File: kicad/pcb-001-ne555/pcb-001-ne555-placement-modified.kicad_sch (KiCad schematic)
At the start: 14 parts, among them J1 +5 V / GND power input, U1 NE555D

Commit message: Update project files 2026-08-16 01:39:38
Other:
- moved on the sheet: R3
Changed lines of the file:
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@@
+	)
+	(junction
+		(at 194.31 102.87)
+		(diameter 0)
+		(color 0 0 0 0)
 	)
 	(junction
@@
 	)
 	(junction
-		(at 194.31 102.87)
-		(diameter 0)
-		(color 0 0 0 0)
-	)
-	(junction
 		(at 129.54 99.06)
 		(diameter 0)
@@
 	(wire
 		(pts
+			(xy 194.31 102.87) (xy 198.12 102.87)
+		)
+		(stroke
+			(width 0)
+			(type default)
+		)
+	)
+	(wire
+		(pts
 			(xy 186.69 102.87) (xy 194.31 102.87)
 		)
@@
 	(wire
 		(pts
-			(xy 209.55 102.87) (xy 209.55 106.68)
-		)
-		(stroke
-			(width 0)
-			(type default)
-		)
-	)
-	(wire
-		(pts
-			(xy 194.31 102.87) (xy 200.66 102.87)
+			(xy 207.01 102.87) (xy 207.01 106.68)
 		)
 		(stroke
@@
 	(wire
 		(pts
-			(xy 208.28 102.87) (xy 209.55 102.87)
+			(xy 205.74 102.87) (xy 207.01 102.87)
 		)
 		(stroke
@@
 		)
 		(instances
-			(project "pcb-001-ne555"
+			(project "pcb-001-ne555-placement-modified"
 				(path "/b0c8241f-7280-4983-bb24-fcd4e712ed60"
 					(reference "#PWR04")
@@
 		)
 		(instances
-			(project "pcb-001-ne555"
+			(project "pcb-001-ne555-placement-modified"
 				(path "/b0c8241f-7280-4983-bb24-fcd4e712ed60"
 					(reference "U1")
@@
 		)
 		(property "Value" "PWR_FLAG"
-			(at 145.796 110.744 0)
+			(at 145.288 110.744 0)
 			(show_name no)
 			(do_not_autoplace no)
@@
 		)
 		(instances
-			(project "pcb-001-ne555"
+			(project "pcb-001-ne555-placement-modified"
 				(path "/b0c8241f-7280-4983-bb24-fcd4e712ed60"
 					(reference "#FLG01")
@@
 		)
 		(instances
-			(project "pcb-001-ne555"
+			(project "pcb-001-ne555-placement-modified"
 				(path "/b0c8241f-7280-4983-bb24-fcd4e712ed60"
 					(reference "TP1")
@@
 		)
 		(instances
-			(project "pcb-001-ne555"
+			(project "pcb-001-ne555-placement-modified"
 				(path "/b0c8241f-7280-4983-bb24-fcd4e712ed60"
 					(reference "C3")
@@
 	(symbol
 		(lib_id "power:GND")
-		(at 209.55 106.68 0)
+		(at 207.01 106.68 0)
 		(unit 1)
 		(body_style 1)
@@
 		(fields_autoplaced yes)
 		(property "Reference" "#PWR010"
-			(at 209.55 113.03 0)
+			(at 207.01 113.03 0)
 			(hide yes)
 			(show_name no)
@@
 		)
 		(property "Value" "GND"
-			(at 209.55 111.76 0)
+			(at 207.01 111.76 0)
 			(show_name no)
 			(do_not_autoplace no)
@@
 		)
 		(property "Footprint" ""
-			(at 209.55 106.68 0)
+			(at 207.01 106.68 0)
 			(hide yes)
 			(show_name no)
@@
 		)
 		(property "Datasheet" ""
-			(at 209.55 106.68 0)
+			(at 207.01 106.68 0)
 			(hide yes)
 			(show_name no)
@@
 		)
 		(property "Description" "Power symbol creates a global label with name \"GND\" , ground"
-			(at 209.55 106.68 0)
+			(at 207.01 106.68 0)
 			(hide yes)
 			(show_name no)
@@
 		)
 		(instances
-			(project "pcb-001-ne555"
+			(project "pcb-001-ne555-placement-modified"
 				(path "/b0c8241f-7280-4983-bb24-fcd4e712ed60"
 					(reference "#PWR010")
@@
 		)
 		(instances
-			(project "pcb-001-ne555"
+			(project "pcb-001-ne555-placement-modified"
 				(path "/b0c8241f-7280-4983-bb24-fcd4e712ed60"
 					(reference "C2")
@@
 		)
 		(instances
-			(project "pcb-001-ne555"
+			(project "pcb-001-ne555-placement-modified"
 				(path "/b0c8241f-7280-4983-bb24-fcd4e712ed60"
 					(reference "R2")
@@
 		)
 		(instances
-			(project "pcb-001-ne555"
+			(project "pcb-001-ne555-placement-modified"
 				(path "/b0c8241f-7280-4983-bb24-fcd4e712ed60"
 					(reference "R1")
@@
 		)
 		(instances
-			(project "pcb-001-ne555"
+			(project "pcb-001-ne555-placement-modified"
 				(path "/b0c8241f-7280-4983-bb24-fcd4e712ed60"
 					(reference "TP3")
@@
 	(symbol
 		(lib_id "Device:R")
-		(at 204.47 102.87 90)
+		(at 201.93 102.87 90)
 		(unit 1)
 		(body_style 1)
@@
 		(fields_autoplaced yes)
 		(property "Reference" "R3"
-			(at 204.47 96.52 90)
+			(at 201.93 96.52 90)
 			(show_name no)
 			(do_not_autoplace no)
@@
 		)
 		(property "Value" "330 Ohm"
-			(at 204.47 99.06 90)
+			(at 201.93 99.06 90)
 			(show_name no)
 			(do_not_autoplace no)
@@
 		)
 		(property "Footprint" "Resistor_THT:R_Axial_DIN0207_L6.3mm_D2.5mm_P10.16mm_Horizontal"
-			(at 204.47 104.648 90)
+			(at 201.93 104.648 90)
 			(hide yes)
 			(show_name no)
@@
 		)
 		(property "Datasheet" ""
-			(at 204.47 102.87 0)
+			(at 201.93 102.87 0)
 			(hide yes)
 			(show_name no)
@@
 		)
 		(property "Description" "Resistor"
-			(at 204.47 102.87 0)
+			(at 201.93 102.87 0)
 			(hide yes)
 			(show_name no)
@@
 		)
 		(instances
-			(project "pcb-001-ne555"
+			(project "pcb-001-ne555-placement-modified"
 				(path "/b0c8241f-7280-4983-bb24-fcd4e712ed60"
 					(reference "R3")
@@
 		)
 		(instances
-			(project "pcb-001-ne555"
+			(project "pcb-001-ne555-placement-modified"
 				(path "/b0c8241f-7280-4983-bb24-fcd4e712ed60"
 					(reference "TP2")
@@
 		)
 		(property "Value" "PWR_FLAG"
-			(at 136.906 118.618 0)
+			(at 140.462 118.618 0)
 			(show_name no)
 			(do_not_autoplace no)
@@
 		)
 		(instances
-			(project "pcb-001-ne555"
+			(project "pcb-001-ne555-placement-modified"
 				(path "/b0c8241f-7280-4983-bb24-fcd4e712ed60"
 					(reference "#FLG02")
@@
 		)
 		(instances
-			(project "pcb-001-ne555"
+			(project "pcb-001-ne555-placement-modified"
 				(path "/b0c8241f-7280-4983-bb24-fcd4e712ed60"
 					(reference "#PWR02")
@@
 		)
 		(instances
-			(project "pcb-001-ne555"
+			(project "pcb-001-ne555-placement-modified"
 				(path "/b0c8241f-7280-4983-bb24-fcd4e712ed60"
 					(reference "RV1")
@@
 		)
 		(instances
-			(project "pcb-001-ne555"
+			(project "pcb-001-ne555-placement-modified"
 				(path "/b0c8241f-7280-4983-bb24-fcd4e712ed60"
 					(reference "TP4")
@@
 		)
 		(instances
-			(project "pcb-001-ne555"
+			(project "pcb-001-ne555-placement-modified"
 				(path "/b0c8241f-7280-4983-bb24-fcd4e712ed60"
 					(reference "#PWR08")
@@
 		)
 		(instances
-			(project "pcb-001-ne555"
+			(project "pcb-001-ne555-placement-modified"
 				(path "/b0c8241f-7280-4983-bb24-fcd4e712ed60"
 					(reference "#PWR07")
@@
 		)
 		(instances
-			(project "pcb-001-ne555"
+			(project "pcb-001-ne555-placement-modified"
 				(path "/b0c8241f-7280-4983-bb24-fcd4e712ed60"
 					(reference "D1")
@@
 		)
 		(instances
-			(project "pcb-001-ne555"
+			(project "pcb-001-ne555-placement-modified"
 				(path "/b0c8241f-7280-4983-bb24-fcd4e712ed60"
 					(reference "#PWR05")
@@
 		)
 		(instances
-			(project "pcb-001-ne555"
+			(project "pcb-001-ne555-placement-modified"
 				(path "/b0c8241f-7280-4983-bb24-fcd4e712ed60"
 					(reference "#PWR03")
@@
 		)
 		(instances
-			(project "pcb-001-ne555"
+			(project "pcb-001-ne555-placement-modified"
 				(path "/b0c8241f-7280-4983-bb24-fcd4e712ed60"
 					(reference "C1")
@@
 		)
 		(instances
-			(project "pcb-001-ne555"
+			(project "pcb-001-ne555-placement-modified"
 				(path "/b0c8241f-7280-4983-bb24-fcd4e712ed60"
 					(reference "#PWR01")
@@
 		)
 		(instances
-			(project "pcb-001-ne555"
+			(project "pcb-001-ne555-placement-modified"
 				(path "/b0c8241f-7280-4983-bb24-fcd4e712ed60"
 					(reference "J1")
@@
 		)
 		(instances
-			(project "pcb-001-ne555"
+			(project "pcb-001-ne555-placement-modified"
 				(path "/b0c8241f-7280-4983-bb24-fcd4e712ed60"
 					(reference "#PWR06")
@@
 		)
 		(instances
-			(project "pcb-001-ne555"
+			(project "pcb-001-ne555-placement-modified"
 				(path "/b0c8241f-7280-4983-bb24-fcd4e712ed60"
 					(reference "#PWR09")

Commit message: Update project files 2026-08-16 14:48:06
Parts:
- J1: symbol Connector_Generic:Conn_01x02 -> Connector:Screw_Terminal_01x02
- U1: value NE555D -> NE555P; symbol Timer:NE555D -> Timer:NE555P
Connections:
- net VOUT: no longer D1.1 (K), R3.1
- new net: D1.1 (K), R3.1
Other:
- moved on the sheet: TP2
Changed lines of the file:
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@@
-	)
-	(junction
-		(at 194.31 102.87)
-		(diameter 0)
-		(color 0 0 0 0)
 	)
 	(junction
@@
 	)
 	(junction
-		(at 181.61 102.87)
+		(at 129.54 96.52)
 		(diameter 0)
 		(color 0 0 0 0)
@@
 	)
 	(junction
-		(at 186.69 102.87)
+		(at 181.61 102.87)
 		(diameter 0)
 		(color 0 0 0 0)
 	)
-	(junction
-		(at 129.54 99.06)
-		(diameter 0)
-		(color 0 0 0 0)
-	)
 	(wire
 		(pts
@@
 	(wire
 		(pts
-			(xy 125.73 99.06) (xy 129.54 99.06)
+			(xy 124.46 96.52) (xy 129.54 96.52)
 		)
 		(stroke
@@
 	(wire
 		(pts
-			(xy 116.84 101.6) (xy 116.84 106.68)
-		)
-		(stroke
-			(width 0)
-			(type default)
-		)
-	)
-	(wire
-		(pts
-			(xy 125.73 106.68) (xy 125.73 99.06)
-		)
-		(stroke
-			(width 0)
-			(type default)
-		)
-	)
-	(wire
-		(pts
 			(xy 157.48 107.95) (xy 160.02 107.95)
 		)
@@
 	(wire
 		(pts
-			(xy 116.84 106.68) (xy 125.73 106.68)
-		)
-		(stroke
-			(width 0)
-			(type default)
-		)
-	)
-	(wire
-		(pts
 			(xy 139.7 116.84) (xy 143.51 116.84)
 		)
@@
 	(wire
 		(pts
-			(xy 129.54 96.52) (xy 129.54 99.06)
+			(xy 129.54 96.52) (xy 129.54 100.33)
 		)
 		(stroke
@@
 	(wire
 		(pts
-			(xy 186.69 102.87) (xy 194.31 102.87)
-		)
-		(stroke
-			(width 0)
-			(type default)
-		)
-	)
-	(wire
-		(pts
 			(xy 102.87 90.17) (xy 106.68 90.17)
 		)
@@
 	(wire
 		(pts
-			(xy 129.54 99.06) (xy 129.54 100.33)
-		)
-		(stroke
-			(width 0)
-			(type default)
-		)
-	)
-	(wire
-		(pts
 			(xy 148.59 100.33) (xy 148.59 97.79)
 		)
@@
 		(pts
 			(xy 205.74 102.87) (xy 207.01 102.87)
+		)
+		(stroke
+			(width 0)
+			(type default)
+		)
+	)
+	(wire
+		(pts
+			(xy 124.46 96.52) (xy 124.46 104.14)
 		)
 		(stroke
@@
 		(in_pos_files yes)
 		(dnp no)
-		(fields_autoplaced yes)
 		(property "Reference" "#PWR04"
 			(at 139.7 106.68 0)
@@
 		)
 		(property "Value" "+5V"
-			(at 139.7 97.79 0)
+			(at 139.446 99.314 0)
 			(show_name no)
 			(do_not_autoplace no)
@@
 	)
 	(symbol
-		(lib_id "Timer:NE555D")
+		(lib_id "Timer:NE555P")
 		(at 170.18 102.87 0)
 		(unit 1)
@@
 			)
 		)
-		(property "Value" "NE555D"
-			(at 173.736 105.156 0)
-			(show_name no)
-			(do_not_autoplace no)
-			(effects
-				(font
-					(size 1.27 1.27)
-				)
+		(property "Value" "NE555P"
+			(at 169.926 105.156 0)
+			(show_name no)
+			(do_not_autoplace no)
+			(effects
+				(font
+					(size 1.27 1.27)
+				)
+				(justify left)
 			)
 		)
@@
 			)
 		)
-		(property "Description" "Precision Timers, 555 compatible, SOIC-8"
+		(property "Description" "Precision Timers, 555 compatible, PDIP-8"
 			(at 170.18 124.46 0)
 			(hide yes)
@@
 		(in_pos_files yes)
 		(dnp no)
-		(fields_autoplaced yes)
 		(property "Reference" "TP1"
-			(at 137.16 71.6279 0)
+			(at 133.35 71.12 0)
 			(show_name no)
 			(do_not_autoplace no)
@@
 		)
 		(property "Value" "+5 V"
-			(at 137.16 74.1679 0)
+			(at 131.826 77.216 0)
 			(show_name no)
 			(do_not_autoplace no)
@@
 		(dnp no)
 		(property "Reference" "C2"
-			(at 153.67 75.184 0)
+			(at 158.75 80.772 0)
 			(show_name no)
 			(do_not_autoplace no)
@@
 		)
 		(property "Value" "10 nF"
-			(at 153.67 77.724 0)
+			(at 157.48 84.836 0)
 			(show_name no)
 			(do_not_autoplace no)
@@
 		(in_pos_files yes)
 		(dnp no)
-		(fields_autoplaced yes)
 		(property "Reference" "R2"
-			(at 119.3801 81.28 0)
+			(at 116.84 76.708 90)
 			(show_name no)
 			(do_not_autoplace no)
@@
 		)
 		(property "Value" "10 kOhm"
-			(at 116.8401 81.28 0)
+			(at 114.046 81.026 90)
 			(show_name no)
 			(do_not_autoplace no)
@@
 		(in_pos_files yes)
 		(dnp no)
-		(fields_autoplaced yes)
 		(property "Reference" "R1"
-			(at 130.8101 81.28 0)
+			(at 128.27 76.708 90)
 			(show_name no)
 			(do_not_autoplace no)
@@
 		)
 		(property "Value" "10 kOhm"
-			(at 128.2701 81.28 0)
+			(at 125.222 81.026 90)
 			(show_name no)
 			(do_not_autoplace no)
@@
 		(in_pos_files yes)
 		(dnp no)
-		(fields_autoplaced yes)
 		(property "Reference" "TP3"
-			(at 184.15 97.0279 0)
+			(at 180.34 96.52 0)
 			(show_name no)
 			(do_not_autoplace no)
@@
 		)
 		(property "Value" "VOUT"
-			(at 184.15 99.5679 0)
+			(at 179.324 104.648 0)
 			(show_name no)
 			(do_not_autoplace no)
@@
 		(in_pos_files yes)
 		(dnp no)
-		(fields_autoplaced yes)
 		(property "Reference" "R3"
-			(at 201.93 96.52 90)
+			(at 201.93 100.584 90)
 			(show_name no)
 			(do_not_autoplace no)
@@
 		)
 		(property "Value" "330 Ohm"
-			(at 201.93 99.06 90)
+			(at 201.93 105.156 90)
 			(show_name no)
 			(do_not_autoplace no)
@@
 	(symbol
 		(lib_id "Connector:TestPoint")
-		(at 116.84 101.6 0)
+		(at 124.46 104.14 180)
 		(unit 1)
 		(body_style 1)
@@
 		(fields_autoplaced yes)
 		(property "Reference" "TP2"
-			(at 119.38 97.0279 0)
-			(show_name no)
-			(do_not_autoplace no)
-			(effects
-				(font
-					(size 1.27 1.27)
-				)
-				(justify left)
+			(at 127 106.1719 0)
+			(show_name no)
+			(do_not_autoplace no)
+			(effects
+				(font
+					(size 1.27 1.27)
+				)
+				(justify right)
 			)
 		)
 		(property "Value" "GND"
-			(at 119.38 99.5679 0)
-			(show_name no)
-			(do_not_autoplace no)
-			(effects
-				(font
-					(size 1.27 1.27)
-				)
-				(justify left)
+			(at 127 108.7119 0)
+			(show_name no)
+			(do_not_autoplace no)
+			(effects
+				(font
+					(size 1.27 1.27)
+				)
+				(justify right)
 			)
 		)
 		(property "Footprint" "TestPoint:TestPoint_THTPad_D2.0mm_Drill1.0mm"
-			(at 121.92 101.6 0)
+			(at 119.38 104.14 0)
 			(hide yes)
 			(show_name no)
@@
 		)
 		(property "Datasheet" ""
-			(at 121.92 101.6 0)
+			(at 119.38 104.14 0)
 			(hide yes)
 			(show_name no)
@@
 		)
 		(property "Description" "test point"
-			(at 116.84 101.6 0)
+			(at 124.46 104.14 0)
 			(hide yes)
 			(show_name no)
@@
 		(in_pos_files yes)
 		(dnp no)
-		(fields_autoplaced yes)
 		(property "Reference" "#PWR02"
 			(at 129.54 106.68 0)
@@
 		)
 		(property "Value" "GND"
-			(at 129.54 105.41 0)
+			(at 130.048 100.584 0)
 			(show_name no)
 			(do_not_autoplace no)
@@
 		(in_pos_files yes)
 		(dnp no)
-		(fields_autoplaced yes)
 		(property "Reference" "RV1"
-			(at 107.9501 76.2 0)
+			(at 110.49 82.042 90)
 			(show_name no)
 			(do_not_autoplace no)
@@
 		)
 		(property "Value" "100 kOhm"
-			(at 105.4101 76.2 0)
+			(at 111.506 75.692 90)
 			(show_name no)
 			(do_not_autoplace no)
@@
 		(dnp no)
 		(property "Reference" "TP4"
-			(at 111.76 89.916 0)
+			(at 109.982 93.98 0)
 			(show_name no)
 			(do_not_autoplace no)
@@
 		)
 		(property "Value" "VCAP"
-			(at 112.522 93.472 0)
+			(at 109.22 97.79 0)
 			(show_name no)
 			(do_not_autoplace no)
@@
 		(in_pos_files yes)
 		(dnp no)
-		(fields_autoplaced yes)
 		(property "Reference" "#PWR08"
 			(at 132.08 78.74 0)
@@
 		)
 		(property "Value" "+5V"
-			(at 140.97 78.74 0)
+			(at 136.652 80.772 90)
 			(show_name no)
 			(do_not_autoplace no)
@@
 		)
 		(property "Value" "GND"
-			(at 156.21 109.728 0)
+			(at 153.924 113.03 0)
 			(show_name no)
 			(do_not_autoplace no)
@@
 		(dnp no)
 		(property "Reference" "D1"
-			(at 193.548 97.282 0)
+			(at 190.5 100.076 0)
 			(show_name no)
 			(do_not_autoplace no)
@@
 		)
 		(property "Value" "red LED"
-			(at 193.548 99.314 0)
+			(at 190.754 105.156 0)
 			(show_name no)
 			(do_not_autoplace no)
@@
 		(in_pos_files yes)
 		(dnp no)
-		(fields_autoplaced yes)
 		(property "Reference" "#PWR03"
 			(at 151.13 90.17 0)
@@
 		)
 		(property "Value" "+5V"
-			(at 151.13 81.28 0)
+			(at 150.876 82.804 0)
 			(show_name no)
 			(do_not_autoplace no)
@@
 		(in_pos_files yes)
 		(dnp no)
-		(fields_autoplaced yes)
 		(property "Reference" "#PWR01"
 			(at 166.37 86.36 0)
@@
 		)
 		(property "Value" "+5V"
-			(at 166.37 77.47 0)
+			(at 166.37 78.994 0)
 			(show_name no)
 			(do_not_autoplace no)
@@
 	)
 	(symbol
-		(lib_id "Connector_Generic:Conn_01x02")
+		(lib_id "Connector:Screw_Terminal_01x02")
 		(at 148.59 114.3 0)
 		(unit 1)
@@
 			)
 		)
-		(property "Description" "Generic connector, single row, 01x02, script generated (kicad-library-utils/schlib/autogen/connector/)"
+		(property "Description" "Generic screw terminal, single row, 01x02, script generated (kicad-library-utils/schlib/autogen/connector/)"
 			(at 148.59 114.3 0)
 			(hide yes)

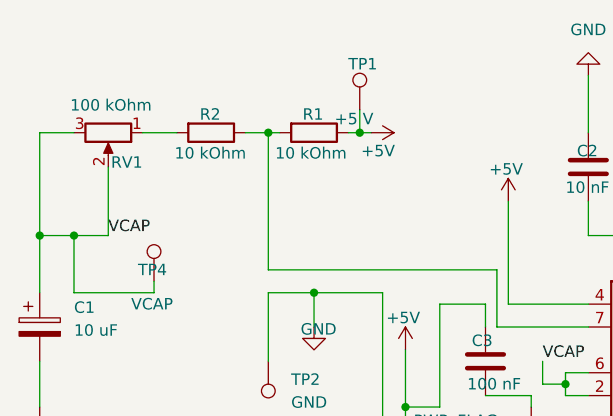
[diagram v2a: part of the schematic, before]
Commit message: docs: publish final PCB-001 engineering record
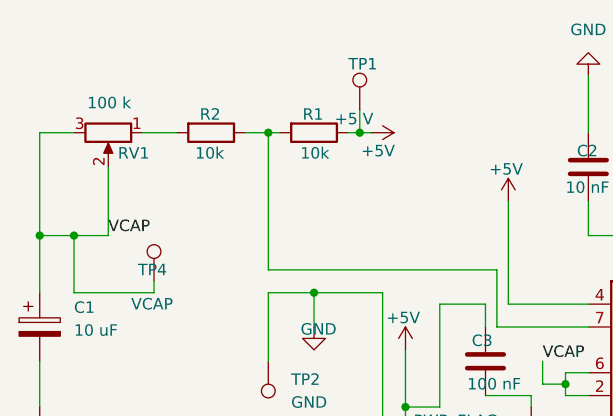
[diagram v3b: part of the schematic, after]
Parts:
- C1: MPN (none) -> ECEA1VKA100; Manufacturer (none) -> Panasonic Industry
- C2: MPN (none) -> K103K10X7RF53H5; Manufacturer (none) -> Vishay BCcomponents
- C3: MPN (none) -> K104K10X7RF53H5; Manufacturer (none) -> Vishay BCcomponents
- D1: MPN (none) -> L-53LID; Manufacturer (none) -> Kingbright
- J1: MPN (none) -> TB007-508-02BE; Manufacturer (none) -> Same Sky
- R1, R2: value 10 kOhm -> 10k; MPN (none) -> MFR-25FBF52-10K; Manufacturer (none) -> YAGEO
- R3: MPN (none) -> MFR-25FBF52-330R; Manufacturer (none) -> YAGEO
- RV1: value 100 kOhm -> 100 k; MPN (none) -> 3386P-1-104LF; Manufacturer (none) -> Bourns
- U1: MPN (none) -> NE555P; Manufacturer (none) -> Texas Instruments
